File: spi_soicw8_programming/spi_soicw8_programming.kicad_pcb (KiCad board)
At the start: 2 copper layers, 19.2 x 15.3 mm, 3 parts, among them P1 CONN_02X04, P2 CONN_01X06

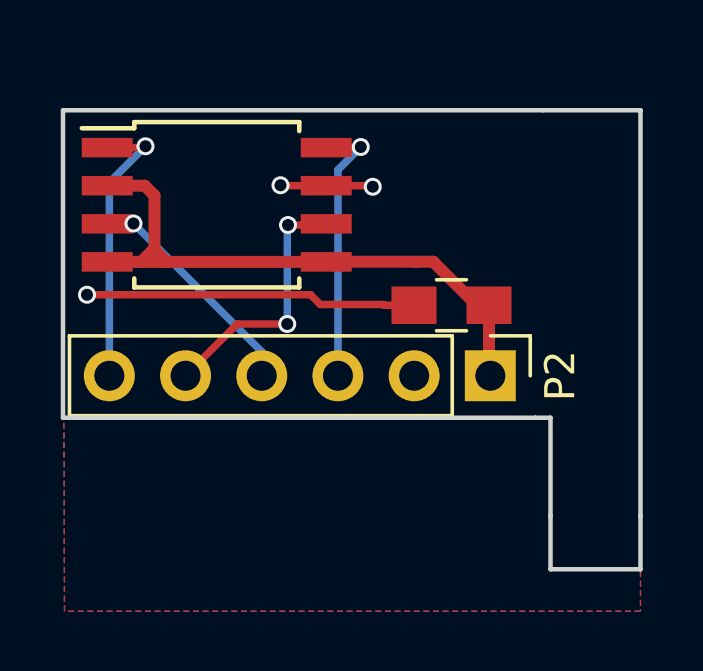
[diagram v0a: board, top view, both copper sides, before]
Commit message: Fixed SPI flash mod board, added silkscreen helpers
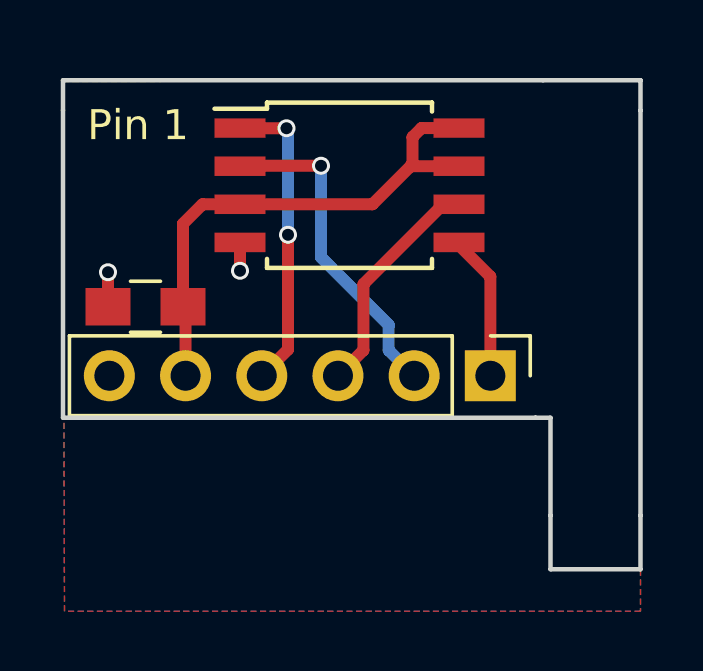
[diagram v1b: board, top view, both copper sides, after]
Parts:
- removed P1: CONN_02X04, Housings_SOIC:SOIJ-8_5.3x5.3mm_Pitch1.27mm
- added U1: 25LC_EEPROM, Housings_SOIC:SOIJ-8_5.3x5.3mm_Pitch1.27mm, F.Cu at (150.3, 104.0)
- moved C1 10.2 mm to (143.5, 108.0)
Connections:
- P2 pad 1: +3V3 -> MOSI
- P2 pad 2: GND -> MISO
- P2 pad 3: MOSI -> CLK
- P2 pad 4: MISO -> CS
- P2 pad 5: CLK -> +3V3
- P2 pad 6: CS -> GND
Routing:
- net GND: track 14.1 -> 2.24 mm, vias 3 -> 2
- net MOSI: track 9.10 -> 4.94 mm, vias 1 -> 0
- net MISO: track 7.72 -> 11.0 mm
- net +3V3: track 20.4 -> 18.3 mm
- net CLK: track 8.71 -> 7.69 mm, vias 2 -> 0
- net CS: track 9.44 -> 10.2 mm, vias 1 -> 2
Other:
- board size 19.2 x 15.3 mm -> 19.2 x 16.3 mm
- board text added: "1"
- board text added: "4 ZeroPhone"
- board text added: "P1"
- board text added: "Pin 1"
- board text added: "SPI flash mod"
- board text added: "^"
- board text added: "cs vcc miso vcc vcc clk gnd mosi"
- board text added: "v1.0"

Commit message: Changing silkscreen text
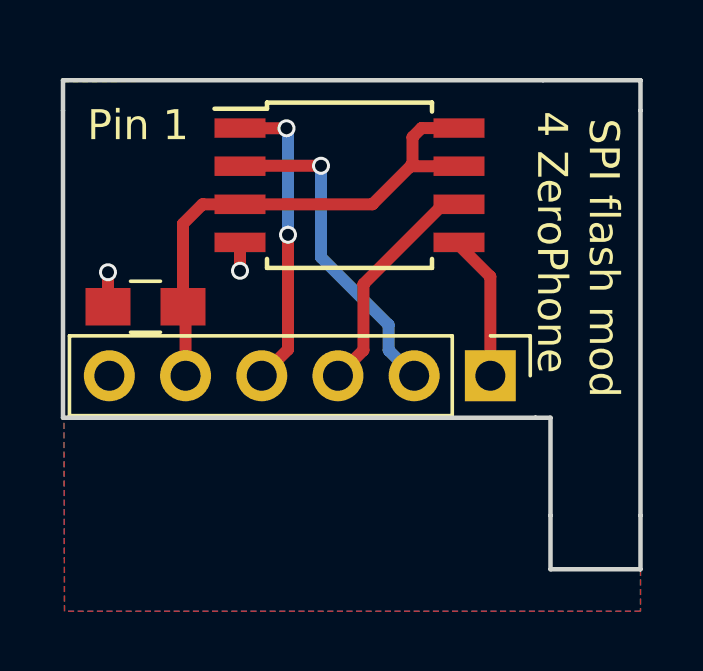
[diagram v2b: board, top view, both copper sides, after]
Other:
- board text added: "v1.1"
- board text removed: "v1.0"
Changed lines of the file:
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@@
-(kicad_pcb (version 4) (host pcbnew 4.0.6)
+(kicad_pcb (version 4) (host pcbnew 4.0.7)
   (general
-    (links 18)
-    (no_connects 16)
+    (links 10)
+    (no_connects 0)
     (area 140.674999 100.424999 160.075001 116.875001)
     (thickness 1.6)
@@
   (page A4)
   (layers
-    (0 F.Cu signal hide)
-    (31 B.Cu signal hide)
+    (0 F.Cu signal)
+    (31 B.Cu signal)
     (32 B.Adhes user)
     (33 F.Adhes user)
@@
     (35 F.Paste user)
     (36 B.SilkS user)
-    (37 F.SilkS user hide)
+    (37 F.SilkS user)
     (38 B.Mask user)
     (39 F.Mask user hide)
@@
   )
   (setup
-    (last_trace_width 0.4)
+    (last_trace_width 0.25)
     (user_trace_width 0.4)
     (trace_clearance 0.2)
@@
     (pad_to_mask_clearance 0.2)
     (aux_axis_origin 160 100.5)
-    (visible_elements 7FFFFDFF)
+    (visible_elements 7FFFFFFF)
     (pcbplotparams
       (layerselection 0x010f0_80000001)
@@
       (net 2 GND))
     (model Pin_Headers.3dshapes/Pin_Header_Angled_1x06_Pitch2.54mm.wrl
-      (at (xyz 0 -0.25 0))
+      (at (xyz 0 0 0))
       (scale (xyz 1 1 1))
-      (rotate (xyz 0 0 90))
+      (rotate (xyz 0 0 0))
     )
   )
@@
     (effects (font (size 1 1) (thickness 0.25)))
   )
-  (gr_text v1.0 (at 142.5 105.25 270) (layer B.SilkS)
+  (gr_text v1.1 (at 142.5 105.25 270) (layer B.SilkS)
     (effects (font (size 1.5 1.5) (thickness 0.3)) (justify mirror))
   )
@@
     (effects (font (size 1 1) (thickness 0.25)) (justify mirror))
   )
-  (gr_text "4 ZeroPhone" (at 156.75 106 270) (layer B.SilkS)
-    (effects (font (size 1 1) (thickness 0.25)) (justify mirror))
-  )
-  (gr_text "SPI flash mod" (at 158.5 106.75 270) (layer B.SilkS)
-    (effects (font (size 1 1) (thickness 0.25)) (justify mirror))
+  (gr_text "4 ZeroPhone" (at 157.05 105.9 270) (layer F.SilkS)
+    (effects (font (size 1 1) (thickness 0.25)))
+  )
+  (gr_text "SPI flash mod" (at 158.775 106.425 270) (layer F.SilkS)
+    (effects (font (size 1 1) (thickness 0.25)))
   )
   (gr_line (start 149.5 101.5) (end 149.5 108.5) (layer B.SilkS) (width 0.2))
